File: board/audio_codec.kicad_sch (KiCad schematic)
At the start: 41 parts, among them U1401 TLV320AIC3110IRHB

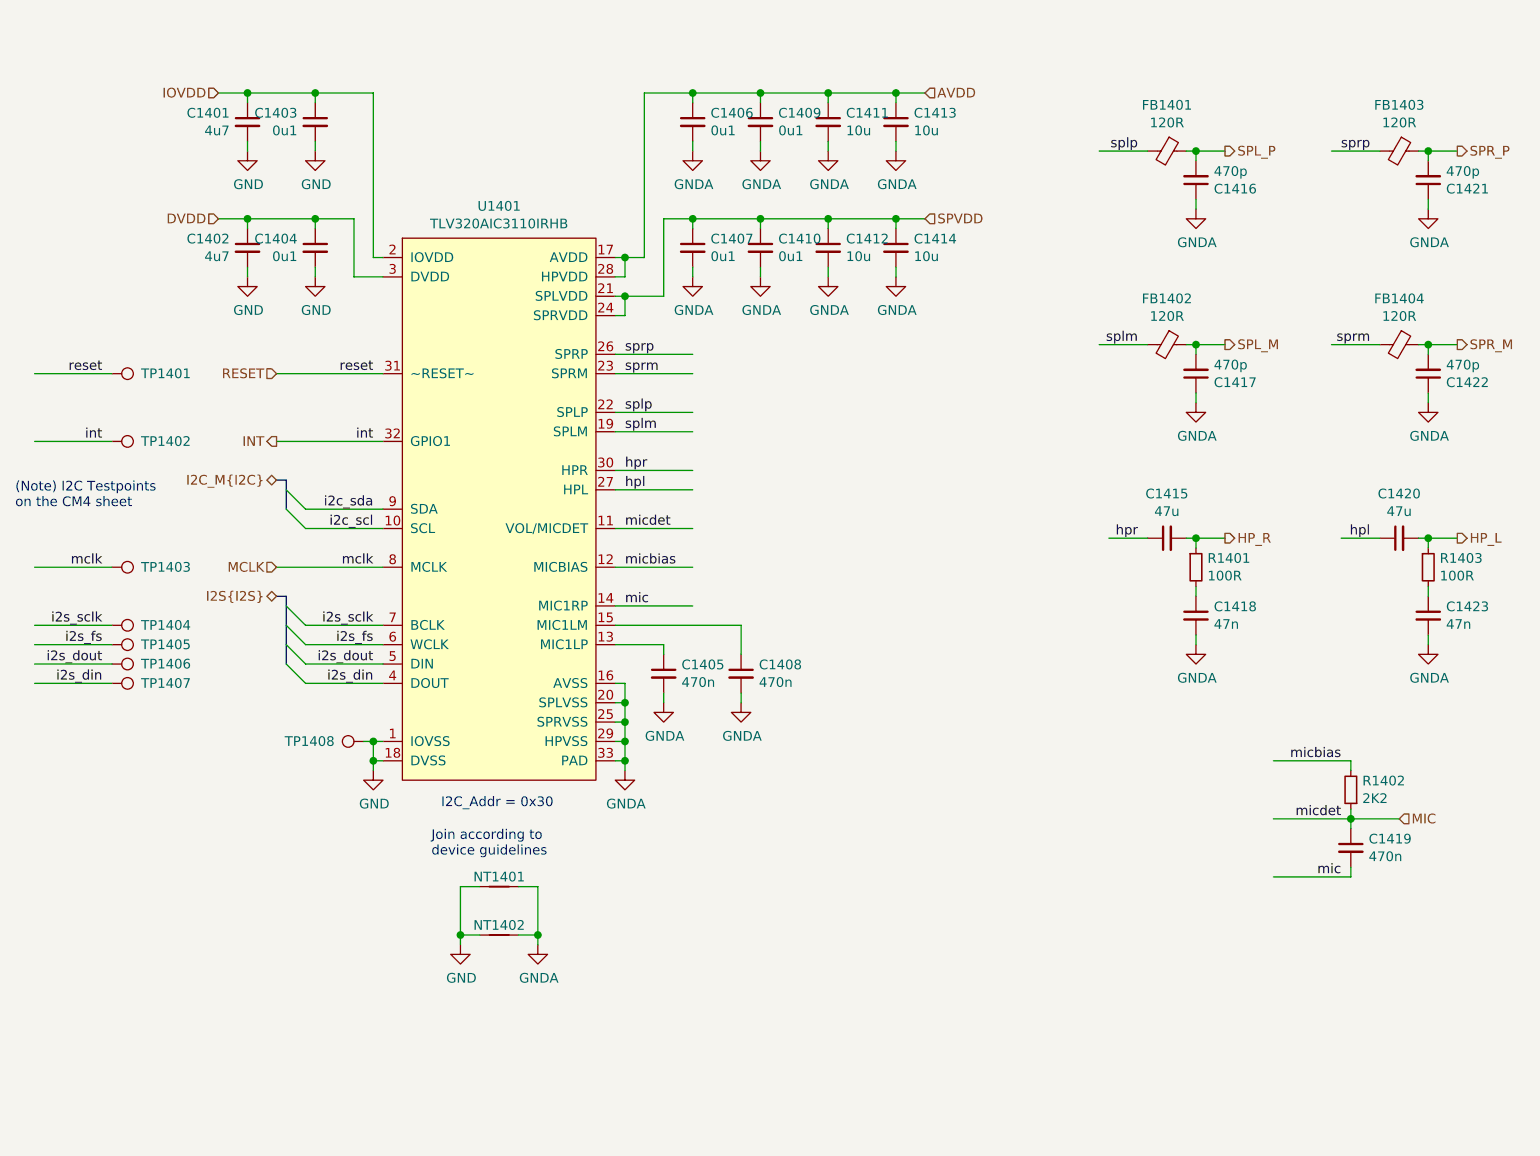
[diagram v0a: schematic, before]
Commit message: Added testpoints and other fixes
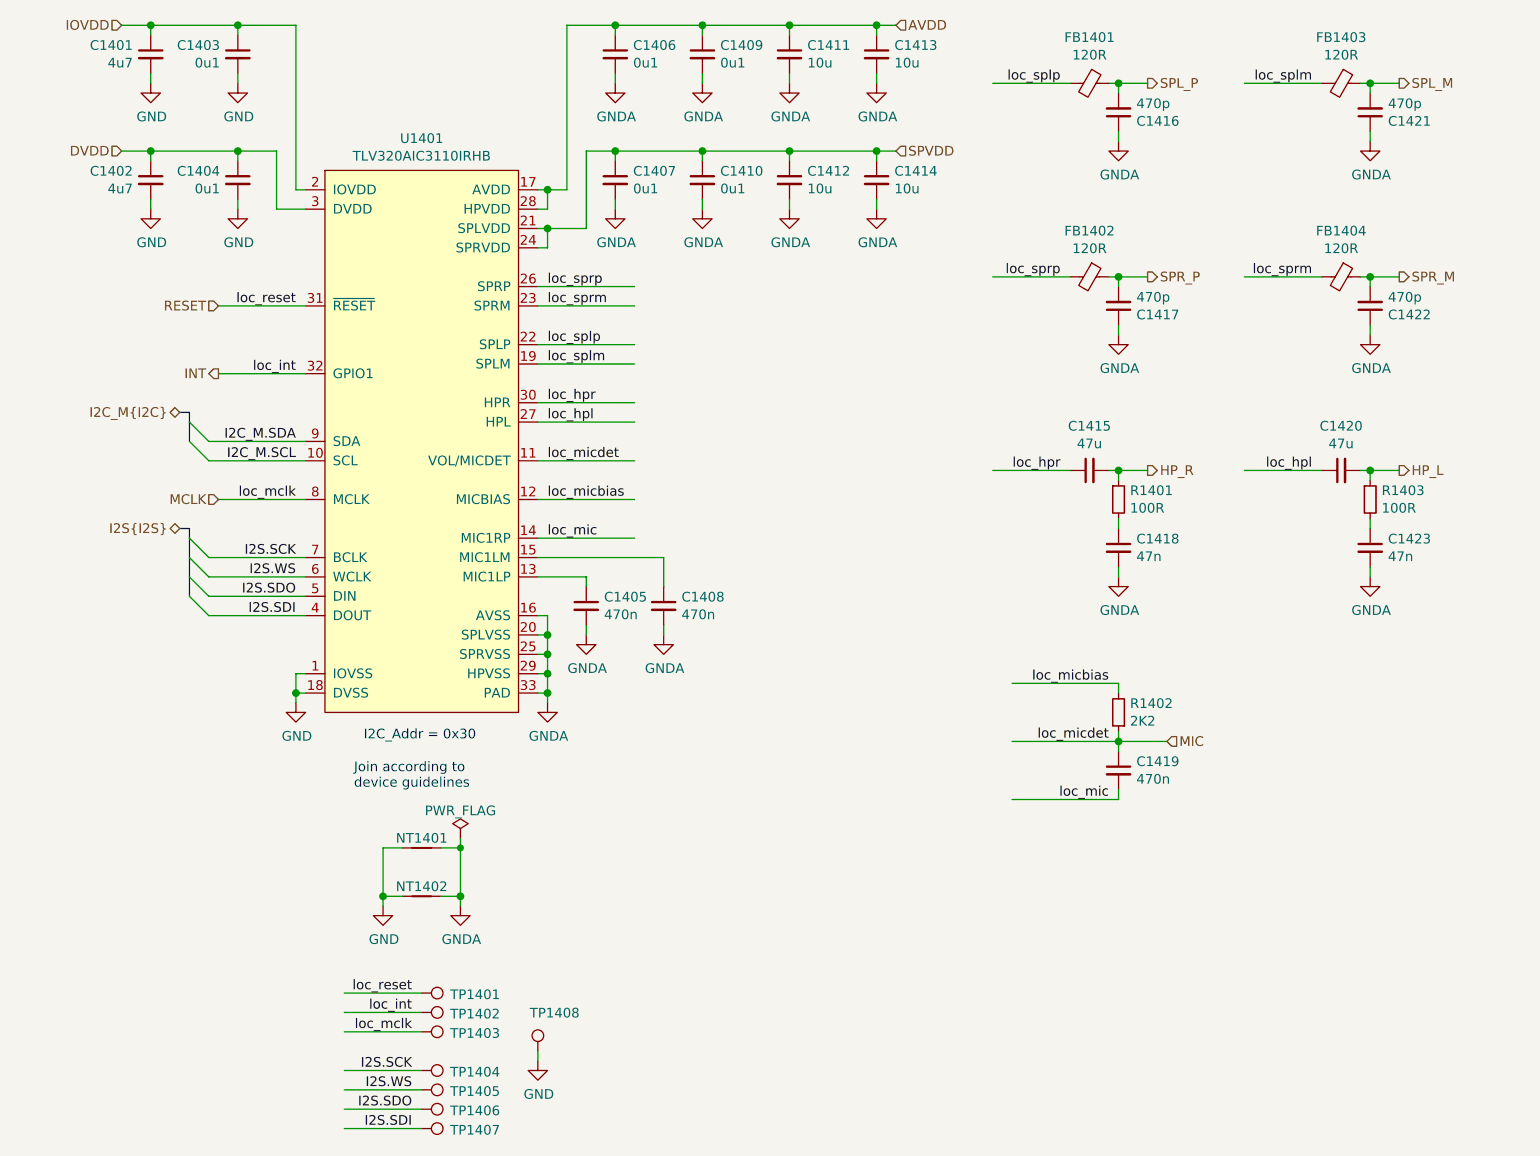
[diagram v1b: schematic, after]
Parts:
- renumbered C1421 to C1417, C1417 to C1421, FB1403 to FB1402, FB1402 to FB1403
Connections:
- net hpl renamed loc_hpl
- net hpr renamed loc_hpr
- net i2c_scl renamed I2C_M.SCL
- net i2c_sda renamed I2C_M.SDA
- net i2s_din renamed I2S.SDI
- net i2s_dout renamed I2S.SDO
- net i2s_fs renamed I2S.WS
- net i2s_sclk renamed I2S.SCK
- net mic renamed loc_mic
- net micbias renamed loc_micbias
- net splm renamed loc_splm
- net splp renamed loc_splp
- net sprm renamed loc_sprm
- net sprp renamed loc_sprp
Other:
- note removed: "(Note) I2C Testpoints on the CM4 sheet"
- moved on the sheet: C1401, C1402, C1403, C1404, C1405, C1406, C1407, C1408, C1409, C1410, C1411, C1412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
